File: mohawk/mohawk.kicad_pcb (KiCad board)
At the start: 2 copper layers, 65 x 30 mm, 50 parts, among them J1 GPIO, J2 SMA, J3 UI Header, J4 DB9 Header, U1 CAT24C256, U2 SC16IS752IPW_128, U4 MAX232, U5 TLV320AIC3204IRHBR, Y1 ASE-1.8432MHz

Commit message: clean up traces; add missing serial resistors for I²S lines
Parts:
- added R16: 27, Resistor_SMD:R_0805_2012Metric, B.Cu at (150.0, 78.2)
- added R17: 27, Resistor_SMD:R_0805_2012Metric, B.Cu at (123.0, 84.0)
- added R18: 27, Resistor_SMD:R_0805_2012Metric, B.Cu at (157.8, 82.0)
- added R19: 27, Resistor_SMD:R_0805_2012Metric, B.Cu at (109.0, 85.5)
- R15: value 0 -> 10
- moved R15 11.2 mm to (106.0, 78.0), turned to 90 degrees
- moved C2 1.60 mm to (111.0, 96.8), turned to -90 degrees
- moved C10 0.87 mm to (109.0, 83.5)
- moved C9 0.87 mm to (109.0, 81.5)
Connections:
- U5 pad 2: GPIO18/PCM.CLK -> Net-(U5-BCLK)
- U5 pad 3: GPIO19/PCM.FS -> Net-(U5-WCLK)
- U5 pad 4: GPIO21/PCM.DOUT -> Net-(U5-DIN_MFP1)
- U5 pad 5: GPIO20/PCM.DIN -> Net-(U5-DOUT_MFP2)
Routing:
- net GPIO19/PCM.FS: track 59.8 -> 3.21 mm, vias 2 -> 0
- net Net-(U5-WCLK): track 0.00 -> 55.4 mm, vias 0 -> 2
- net GPIO21/PCM.DOUT: track 64.0 -> 9.53 mm, vias 2 -> 0
- net Net-(U5-DIN_MFP1): track 0.00 -> 52.9 mm, vias 0 -> 2
- net GPIO18/PCM.CLK: track 32.1 -> 13.1 mm, vias 2 -> 0
- net Net-(U5-BCLK): track 0.00 -> 17.2 mm, vias 0 -> 2
- net Net-(U5-MCLK): track 4.44 -> 18.4 mm, vias 0 -> 2
- net GPIO4/GPCLK0: track 25.1 -> 11.9 mm
- net +3V3: track 183.0 -> 187.2 mm
- net Net-(U5-DOUT_MFP2): track 0.00 -> 3.64 mm
- net GPIO8/SPI0.CE0: track 36.4 -> 39.8 mm
- net GND: track 41.5 -> 38.2 mm, vias 25 -> 23
- net GPIO20/PCM.DIN: track 61.2 -> 63.3 mm
- net GPIO3/SCL1: track 12.8 -> 13.9 mm
- net ID_SCL: track 23.1 -> 22.4 mm
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
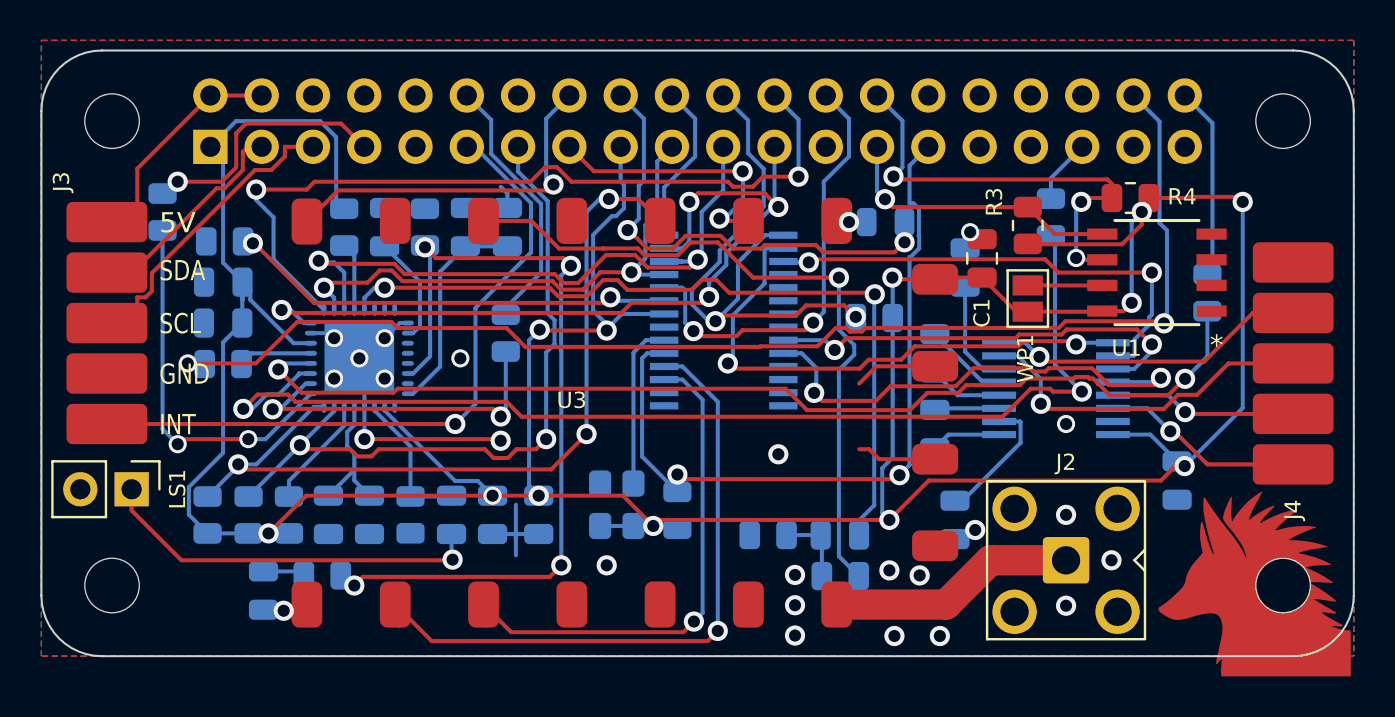
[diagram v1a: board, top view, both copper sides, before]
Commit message: routing cleanups / add renders
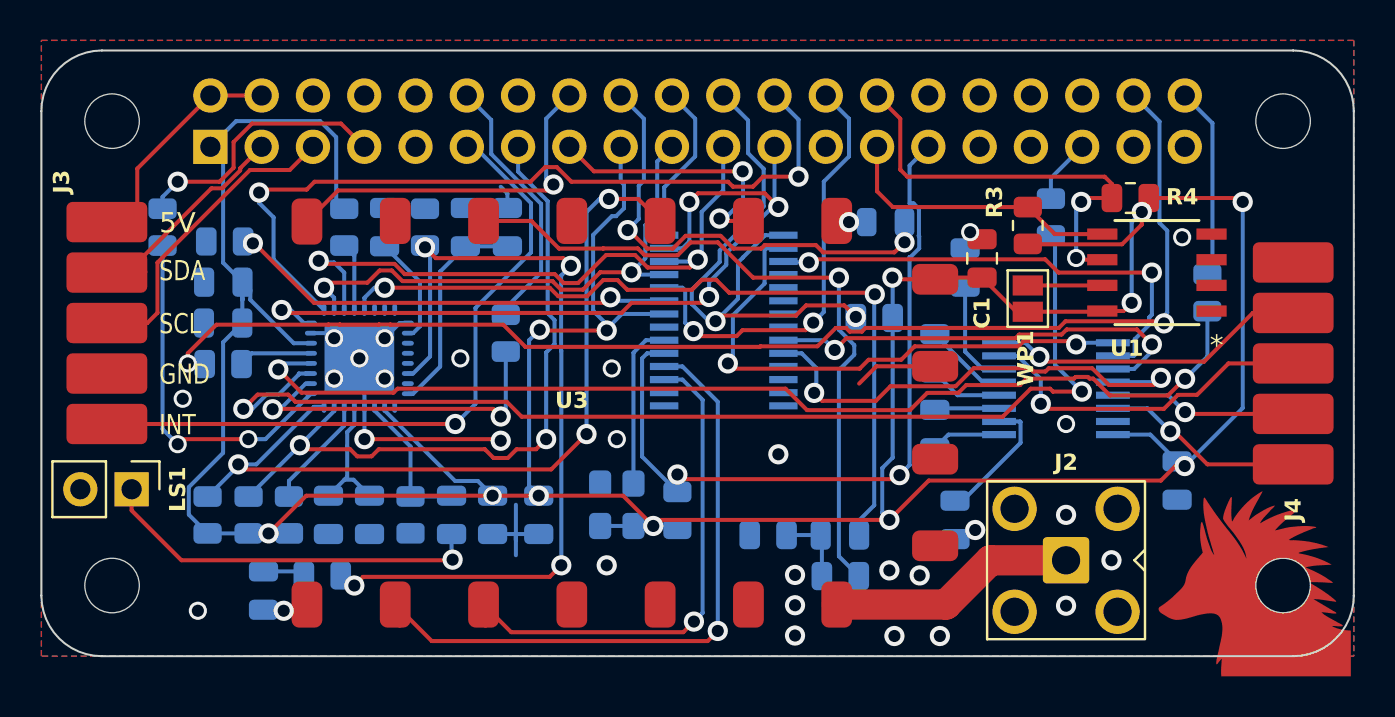
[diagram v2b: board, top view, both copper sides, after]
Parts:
- moved R15 0.75 mm to (106.0, 78.8)
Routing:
- net GND: track 38.2 -> 34.3 mm, vias 23 -> 28
- net GPIO3/SCL1: track 13.9 -> 15.3 mm
- net GPIO4/GPCLK0: track 11.9 -> 13.3 mm
- net ID_SCL: track 22.4 -> 21.6 mm, vias 3 -> 2
- net Net-(U5-MCLK): track 18.4 -> 17.6 mm
- net ID_SDA: vias 1 -> 0

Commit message: more routing clean up; add external power solder pads, add Makefile
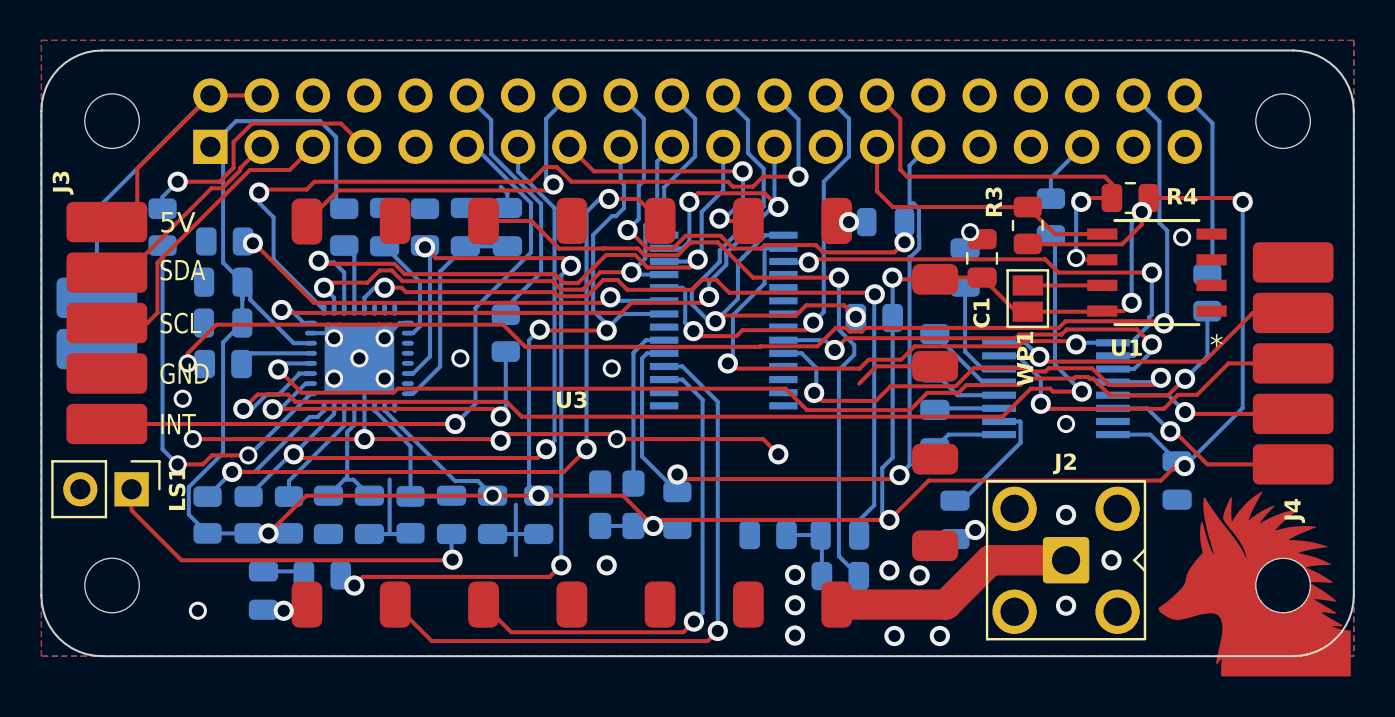
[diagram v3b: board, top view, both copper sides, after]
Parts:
- added J5: +5V In, mohawk:SolderWirePad 1x02, B.Cu at (102.8, 82.2)
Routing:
- net GND: track 34.3 -> 61.8 mm, vias 28 -> 29
- net +5V: track 10.3 -> 23.0 mm
- net Net-(U5-MCLK): track 17.6 -> 19.2 mm
- net PTT: track 41.1 -> 41.9 mm
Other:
- board text added: "+5V GND"

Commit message: add model for SMA connector and regenerate renders
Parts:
- moved R18 3.26 mm to (158.0, 78.8)
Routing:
- net Net-(U5-DIN_MFP1): track 52.9 -> 56.2 mm
- net GPIO21/PCM.DOUT: track 9.53 -> 6.17 mm
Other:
- board text added: "5V GND"
- board text removed: "+5V GND"
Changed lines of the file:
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@@
 			)
 		)
+		(model "/home/sparques/Sync/projects/mohawk/mohawk/lib/SMA-angled.STEP"
+			(offset
+				(xyz 0 0 -4)
+			)
+			(scale
+				(xyz 1 1 1)
+			)
+			(rotate
+				(xyz -0 -0 -0)
+			)
+		)
 	)
 	(footprint "mohawk:DRA818"
@@
 	(footprint "Resistor_SMD:R_0805_2012Metric"
 		(layer "B.Cu")
-		(at 157.75 82 90)
+		(at 158 78.75 90)
 		(descr "Resistor SMD 0805 (2012 Metric), square (rectangular) end terminal, IPC-7351 nominal, (Body size source: IPC-SM-782 page 72, https://www.pcb-3d.com/wordpress/wp-content/uploads/ipc-sm-782a_amendment_1_and_2.pdf)")
 		(tags "resistor")
@@
 		)
 	)
-	(gr_text "+5V GND"
-		(at 106.25 80.75 90)
+	(gr_text "5V GND"
+		(at 106.25 81.25 90)
 		(layer "B.SilkS")
 		(effects
@@
 	)
 	(segment
-		(start 158 80.8375)
-		(end 158 73.6)
-		(width 0.2)
-		(layer "B.Cu")
-		(net "GPIO21{slash}PCM.DOUT")
-	)
-	(segment
 		(start 156.63 72.23)
 		(end 158 73.6)
@@
 	)
 	(segment
-		(start 157.75 81.0875)
-		(end 158 80.8375)
+		(start 158 73.6)
+		(end 158 77.8375)
 		(width 0.2)
 		(layer "B.Cu")
@@
 	)
 	(segment
-		(start 156.646 86.263906)
-		(end 157.75 85.159906)
+		(start 112.032239 85.499999)
+		(end 111.734298 85.79794)
 		(width 0.2)
 		(layer "B.Cu")
@@
 	)
 	(segment
-		(start 112.032239 85.499999)
-		(end 111.734298 85.79794)
+		(start 113.35 85.499999)
+		(end 112.032239 85.499999)
 		(width 0.2)
 		(layer "B.Cu")
@@
 	)
 	(segment
-		(start 157.75 85.159906)
-		(end 157.75 82.9125)
+		(start 156.646 86.263906)
+		(end 158 84.909906)
 		(width 0.2)
 		(layer "B.Cu")
@@
 	)
 	(segment
-		(start 113.35 85.499999)
-		(end 112.032239 85.499999)
+		(start 158 84.909906)
+		(end 158 79.6625)
 		(width 0.2)
 		(layer "B.Cu")

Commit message: add test points for EXT_UART; add 3d model for oscillator
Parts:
- added TP1: TX, TestPoint:TestPoint_Pad_D1.0mm, B.Cu at (156.8, 83.5)
- added TP2: RTS, TestPoint:TestPoint_Pad_D1.0mm, B.Cu at (155.0, 80.0)
- added TP3: RX, TestPoint:TestPoint_Pad_D1.0mm, B.Cu at (156.8, 85.5)
- added TP4: CTS, TestPoint:TestPoint_Pad_D1.0mm, B.Cu at (151.8, 82.5)
- added TP5: V, TestPoint:TestPoint_Pad_D1.0mm, B.Cu at (148.5, 81.5)
- U3: value ~ -> DRA818
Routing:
- net EXT_UART_TX: track 21.8 -> 24.4 mm
- net EXT_UART_CTS: track 27.2 -> 29.3 mm
- net EXT_UART_RTS: track 24.1 -> 25.1 mm
- net GPIO20/PCM.DIN: track 63.5 -> 62.6 mm
- net EXT_UART_RX: track 24.3 -> 25.2 mm
- net Net-(U5-DIN_MFP1): track 56.2 -> 57.0 mm
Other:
- board text added: ":"
- board text added: "Mohawk µHat V1.0"
- board text removed: "Mohawk µHat Ver 1.0"

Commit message: Fix DRA818 foot print; addres DRC errors
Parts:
- C2: value 4.7µF -> 100nF
- R6: value 0 -> 1k
- TP5: value V -> GND
- U3: value DRA818 -> ~
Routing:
- net GPIO25: track 27.9 -> 24.7 mm, vias 2 -> 3
- net GPIO22: track 13.6 -> 12.1 mm
- net EXT_UART_RTS: track 25.1 -> 26.3 mm
- net /UART_RADIO_RX: track 25.8 -> 24.7 mm
- net GPIO24: track 23.5 -> 22.6 mm
- net GPIO9/SPI0.MISO: track 31.3 -> 32.2 mm
- net Net-(U3-AF_OUT): track 35.1 -> 35.8 mm
- net RADIO_SPKR: track 39.5 -> 40.1 mm
- net GND: vias 29 -> 28
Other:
- board text removed: ":"
